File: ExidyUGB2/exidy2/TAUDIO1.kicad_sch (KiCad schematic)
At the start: 40 parts, among them J2 TO LOGIC PCB, Q4 2N3904, Q5 2N3904, U1A 74LS161, U1B 74LS161, U1C_ 74LS04, U1D_ 74LS139, U2A 74LS161, U2B 6331, U2C 74LS374, U2D 74LS374, U3A 74LS161, U3B 74LS161, U3C_ 74LS04, U3D_ 74LS112, U6D 72748

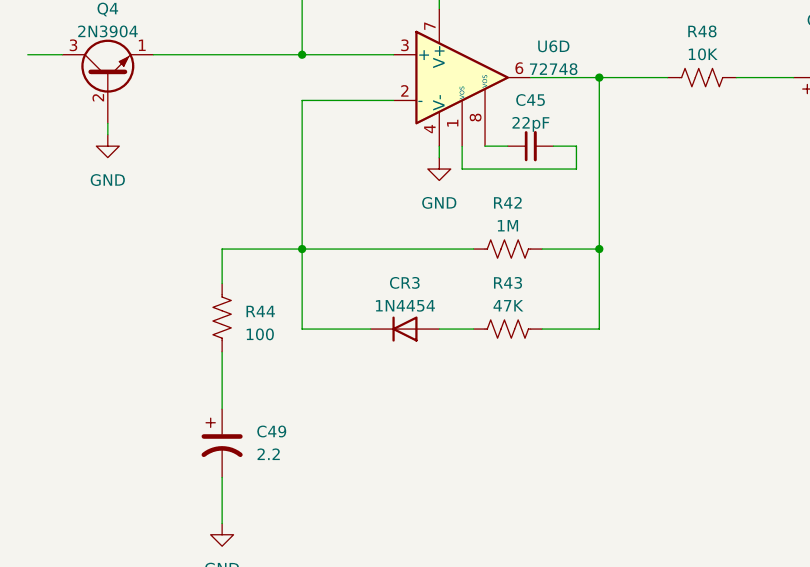
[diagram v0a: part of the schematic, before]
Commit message: Updates to KiCAD8
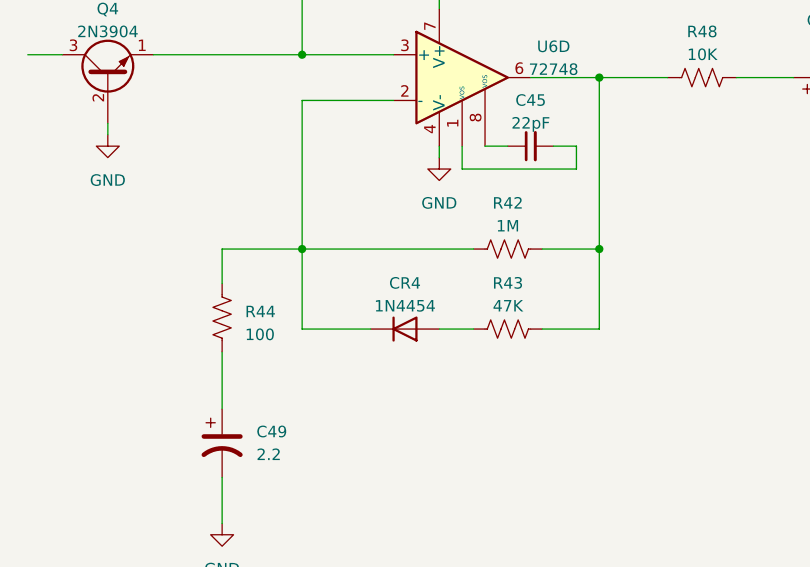
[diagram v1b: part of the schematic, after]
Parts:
- renumbered CR3 to CR4
